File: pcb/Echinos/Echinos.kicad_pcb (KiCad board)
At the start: 4 copper layers, 139.8 x 117.6 mm, 132 parts, among them J1 USB_C_Receptacle_USB2.0, J206 Conn_01x06_Pin, J3 TagConnect_6pins, J301 SATA-7p, J4 FPC_VIK, SW1 SW_Push, SW101 RotaryEncoder_Switch, SW102 SW_Push, SW103 SW_Push, SW105 SW_Push, SW106 SW_Push, SW107 SW_Push, SW108 SW_Push, SW109 SW_Push, SW110 SW_Push, SW111 SW_Push, SW112 SW_Push, SW113 SW_Push, SW114 SW_Push, SW115 SW_Push, SW116 SW_Push, SW117 SW_Push, SW118 SW_Push, SW119 SW_Push, SW120 SW_Push, SW2 SW_Push, U1 RP2040, U2 XC6210B332MR-G, U205 PMW3360DM-T2QU, U206 VRH1902LTX, U3 ESD7L5.0DT5G-N, U4 W25Q128JVS, U7 D3V3F4U6S-7, X1 ASE-12MHz

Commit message: 🚧 [PCB] - Backup of a specific layout around MCU. Modules moved to a specific schematic page.
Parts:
- removed H7, H8, H9: GuardHole, MountingHole:MountingHole_2.2mm_M2_Pad_Via
- added D205: D, Echinos:D_SOD123, F.Cu at (234.8, 92.7)
- added J205: ~, Connector_FFC-FPC:Hirose_FH12-12S-0.5SH_1x12-1MP_P0.50mm_Horizontal, F.Cu at (192.6, 110.6)
- added J207: FPC (module), Connector_FFC-FPC:Hirose_FH12-6S-0.5SH_1x06-1MP_P0.50mm_Horizontal, F.Cu at (226.4, 85.8)
- added J208: FPC (PCB), Connector_FFC-FPC:Hirose_FH12-12S-0.5SH_1x12-1MP_P0.50mm_Horizontal, F.Cu at (111.1, 168.6)
- added J209: Joystick, Echinos:Joystick_Alps_SKRHACE010, F.Cu at (226.4, 96.3)
- moved C206 37.5 mm to (203.3, 94.9)
- moved R207 37.5 mm to (203.3, 102.4)
- moved U205 37.5 mm to (193.8, 97.2)
- moved C205 37.5 mm to (203.3, 92.4)
- moved C207 37.5 mm to (203.3, 97.4)
- moved C208 37.5 mm to (203.3, 99.9)
- moved R208 37.5 mm to (203.3, 104.9)
- moved U206 12.7 mm to (203.1, 109.7)
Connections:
- R208 pad 2: miso1 -> /Modules/miso
- U1 pad 8: /Left Side/RP2040_Left/GPIO6 -> row5
- U205 pad 10: sck1 -> /Modules/sck
- U205 pad 11: mosi1 -> /Modules/mosi
- U205 pad 12: miso1 -> /Modules/miso
- U205 pad 13: csn1 -> /Modules/csn
- U205 pad 9: motion -> /Modules/motion
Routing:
- net row5: track 0.00 -> 18.7 mm, vias 0 -> 1
- net /Left Side/RP2040_Left/GPIO6: track 18.7 -> 0.00 mm, vias 1 -> 0

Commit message: ✨ [PCB] - Make some place to add a FPC connector providing a way to expand the matrix / number of keys or add a joystick and I2C pull-up resistors. Improve routing in order to minimize the number of vias.
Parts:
- R14, R15: footprint Resistor_SMD:R_0805_2012Metric_Pad1.20x1.40mm_HandSolder -> Resistor_SMD:R_0402_1005Metric_Pad0.72x0.64mm_HandSolder
- moved JP2 220.6 mm to (128.6, 145.5), turned to 90 degrees
- moved R14 218.5 mm to (131.2, 144.3), turned to -90 degrees
- moved R15 213.4 mm to (128.6, 142.8), turned to -90 degrees
- moved J208 35.0 mm to (108.3, 133.8), turned to 0 degrees
- moved R13 23.1 mm to (67.2, -72.5), turned to -90 degrees
- moved C1 14.0 mm to (137.2, 136.1), turned to -90 degrees
- moved R2 12.1 mm to (137.2, 133.8)
- moved X1 9.64 mm to (134.0, 134.5), turned to 180 degrees
- moved JP1 7.39 mm to (90.4, -71.5), turned to 90 degrees
- moved R10 3.76 mm to (118.5, 146.9), turned to 90 degrees
- moved R11 3.68 mm to (115.7, 148.8)
- moved R8 3.44 mm to (125.2, 145.8), turned to -90 degrees
- moved C6 2.97 mm to (124.1, 144.5)
- moved C16 2.97 mm to (110.4, 149.1)
- moved U4 2.97 mm to (113.1, 145.2)
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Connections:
- J206 pad 3: sck0 -> mosi0
- J206 pad 4: mosi0 -> miso0
- J206 pad 5: miso0 -> csn0
- J206 pad 6: csn0 -> sck0
- U1 pad 2: rotB -> row5
- U1 pad 3: rotA -> rotB
- U1 pad 4: sck0 -> rotA
- U1 pad 8: row5 -> sck0
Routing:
- net col5: track 155.1 -> 179.4 mm, vias 1 -> 3
- net col4: track 178.1 -> 198.2 mm, vias 1 -> 3
- net col3: track 168.6 -> 188.7 mm
- net row5: track 18.7 -> 38.2 mm, vias 1 -> 2
- net +3.3V: track 309.2 -> 322.5 mm, vias 12 -> 10
- net col2: track 134.6 -> 147.8 mm, vias 1 -> 2
- net adc_1: track 116.8 -> 129.5 mm
- net adc_0: track 110.0 -> 120.1 mm
- net adc_3: track 30.7 -> 40.6 mm
- net /Left Side/SWIO: track 40.3 -> 33.2 mm
- net mosi0: track 16.3 -> 22.4 mm
- net miso0: track 14.6 -> 20.4 mm
- net csn0: track 12.8 -> 18.6 mm
- net Net-(U1-XIN): track 4.43 -> 9.96 mm
- net rotB: track 76.7 -> 82.1 mm
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
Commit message: 🚧 [PCB] - Backup before trying to add 5.0V support.
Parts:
- removed JW108: Joystick, Echinos:Joystick_KSilver_JP19
- added ?: , , F.Cu at (216.8, 98.6)
- added ?: , , F.Cu at (189.2, 98.6)
- added H6: MountHole, Echinos:MountingHole_3mm_Pad_Via, F.Cu at (212.7, 132.2)
- added J1002: Conn_01x06_Female, Connector_PinHeader_2.54mm:PinHeader_1x06_P2.54mm_Vertical, F.Cu at (192.8, 117.3)
- added J1002: Conn_01x06_Female, Connector_PinHeader_2.54mm:PinHeader_1x06_P2.54mm_Vertical, F.Cu at (213.2, 117.1)
- added JP206: i2c1_pullUp, Echinos:SolderJumper_Open_0.8x1.2mm, F.Cu at (2.26, -104.6)
- added R209: 4.7k, Resistor_SMD:R_0402_1005Metric_Pad0.72x0.64mm_HandSolder, F.Cu at (1.95, -93.5)
- added R210: 4.7k, Resistor_SMD:R_0402_1005Metric_Pad0.72x0.64mm_HandSolder, F.Cu at (1.95, -91.5)
- added REF**: vik-module-mounting-small, VIK:vik-module-mounting-small, F.Cu at (203.0, 98.6)
- J206: footprint Connector_PinHeader_2.54mm:PinHeader_1x06_P2.54mm_Vertical -> Connector_PinSocket_2.00mm:PinSocket_1x06_P2.00mm_Horizontal
- U206: value VRH1902LTX -> XC6206P202MR-G; footprint Package_TO_SOT_SMD:SOT-23-5_HandSoldering -> Package_TO_SOT_SMD:SOT-23-3
- moved D205 298.2 mm to (3.66, -95.8)
- moved J207 298.2 mm to (-4.72, -102.7)
- moved J209 298.2 mm to (-4.73, -92.2)
- moved J205 31.2 mm to (209.0, 84.1), turned to 90 degrees
- moved U206 26.4 mm to (195.8, 84.3)
- moved D120 22.9 mm to (190.9, 160.1)
- moved R208 19.8 mm to (201.8, 85.2), turned to -90 degrees
- moved R207 15.5 mm to (195.6, 89.0)
- moved C208 15.0 mm to (195.5, 87.1)
- moved C207 13.0 mm to (198.9, 85.2), turned to -90 degrees
- moved H1 11.9 mm to (212.8, 160.1)
- moved U205 9.24 mm to (203.0, 98.6)
- moved C206 9.00 mm to (194.7, 92.2), turned to 180 degrees
- moved C205 8.78 mm to (194.7, 94.1), turned to 180 degrees
- moved FB2 8.31 mm to (202.7, 153.3)
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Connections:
- net /Left Side/Matrix_Left/joy_108_out renamed Net-(D108-A)
- C207 pad 1: +3.3V -> /Modules/+3.3V_Ball
- C208 pad 1: VDD -> /Modules/VDD_Ball
- D1 pad 2: Net-(D1-A) -> VBUS_Fused
- F1 pad 2: Net-(D1-A) -> VBUS_Fused
- J205 pad 12: +3.3V -> /Modules/+3.3V_Ball
- J208 pad 8: rgb -> adc_0
- J208 pad 9: adc_0 -> rgb
- R205 pad 2: +5V -> VBUS_Fused
- R207 pad 1: VDD -> /Modules/VDD_Ball
- R208 pad 1: +3.3V -> /Modules/+3.3V_Ball
- U205 pad 4: VDD -> /Modules/VDD_Ball
- U205 pad 5: +3.3V -> /Modules/+3.3V_Ball
- U206 pad 1: +3.3V -> GND
- U206 pad 2: GND -> /Modules/VDD_Ball
- U206 pad 3: +3.3V -> /Modules/+3.3V_Ball
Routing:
- net VBUS_Fused: track 0.00 -> 106.2 mm, vias 0 -> 4
- net +5V: track 115.6 -> 11.9 mm, vias 4 -> 0
- net rgb: track 16.1 -> 45.3 mm, vias 2 -> 3
- net row4: track 111.5 -> 88.8 mm, vias 5 -> 4
- net /Left Side/Matrix_Left/joy_120_out: track 3.28 -> 25.0 mm, vias 0 -> 2
- net Net-(D108-A): track 38.3 -> 19.4 mm
- net +3.3V: track 322.5 -> 309.4 mm
- net adc_1: track 129.5 -> 116.5 mm, vias 3 -> 2
- net /Modules/+3.3V_Ball: track 0.00 -> 11.5 mm
- net Net-(U205-VDDPIX): track 0.00 -> 5.82 mm
- net /Modules/miso: track 0.00 -> 5.50 mm
- net adc_0: track 120.1 -> 115.1 mm
- net col2: track 147.8 -> 143.9 mm
- net /Modules/VDD_Ball: track 0.00 -> 3.71 mm
- net col3: track 188.7 -> 185.3 mm
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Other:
- board size 139.8 x 117.6 mm -> 143.4 x 117.6 mm
- board text added: "Kiwano V1.1"

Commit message: ✨ 🚧 [PCB] - Halves are now connected with 5.0V power to be able to expose it to modules (see VIK standard). Update the whole routing to make this happens. VBUS and 5.0V are now split with a schottky diode to still be able to detect when USB is plugged but avoid reverse current in case power comes from the other half. Add ESD events protection to SATA connector.
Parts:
- removed ? (x2): , 
- removed J1002 (x2): Conn_01x06_Female, Connector_PinHeader_2.54mm:PinHeader_1x06_P2.54mm_Vertical
- removed JP1: i2c0_pullUp, Echinos:SolderJumper_Open_0.8x1.2mm
- removed the R12 at (91.0, -80.3)
- removed the R13 at (67.2, -72.5)
- removed REF**: vik-module-mounting-small, VIK:vik-module-mounting-small
- added D4: 1N4148, Diode_SMD:D_SOD-323_HandSoldering, F.Cu at (146.3, 138.5)
- added F2: 500mA, Fuse:Fuse_0603_1608Metric_Pad1.05x0.95mm_HandSolder, F.Cu at (203.7, 150.7)
- U7: value D3V3F4U6S-7 -> SRV05-4; footprint Echinos:D_TVS_SOT-363 -> Package_TO_SOT_SMD:SOT-23-6
- moved D3 84.0 mm to (131.1, 150.2), turned to 0 degrees
- moved C14 82.6 mm to (126.0, 151.9), turned to 0 degrees
- moved R9 82.5 mm to (132.0, 148.7), turned to 180 degrees
- moved JP205 79.1 mm to (132.0, 146.7), turned to -90 degrees
- moved D1 77.6 mm to (122.4, 152.1), turned to 90 degrees
- moved U2 77.2 mm to (126.5, 149.1), turned to 0 degrees
- moved C15 74.5 mm to (129.9, 145.8), turned to 90 degrees
- moved C2 16.1 mm to (144.1, 139.8), turned to 180 degrees
- moved J3 15.1 mm to (143.4, 154.1), turned to 0 degrees
- moved R3 15.0 mm to (144.6, 137.7)
- moved R8 13.1 mm to (137.6, 150.3), turned to 0 degrees
- moved J206 7.16 mm to (109.1, 151.5), turned to 90 degrees
- moved C16 6.26 mm to (104.9, 146.1), turned to 90 degrees
- moved R4 6.09 mm to (116.5, 138.2)
- moved R5 6.03 mm to (116.5, 137.2)
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- renumbered J208 to J2, J301 to J5, R205 to R12, R206 to R13
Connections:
- net /Left Side/QSPI_SCLK renamed /Left Side/RP2040_Left/QSPI_SCLK
- net /Left Side/QSPI_SD0 renamed /Left Side/RP2040_Left/QSPI_SD0
- net /Left Side/QSPI_SD1 renamed /Left Side/RP2040_Left/QSPI_SD1
- net /Left Side/QSPI_SD2 renamed /Left Side/RP2040_Left/QSPI_SD2
- net /Left Side/QSPI_SD3 renamed /Left Side/RP2040_Left/QSPI_SD3
- net /Left Side/QSPI_SS renamed /Left Side/RP2040_Left/QSPI_SS
- net /Left Side/~{RST} renamed /Left Side/RP2040_Left/~{RST}
- D2 pad 1: +5V -> VBUS_Fused
- J2 pad 10: unconnected-(J208-Pin_10-Pad10) -> adc_1
- J2 pad 2: col2 -> col3
- J2 pad 3: col3 -> col4
- J2 pad 4: col4 -> col5
- J2 pad 5: row5 -> col2
- J2 pad 6: col5 -> row5
- J2 pad 7: adc_1 -> unconnected-(J2-Pin_7-Pad7)
- J2 pad 8: adc_0 -> rgb
- J2 pad 9: rgb -> adc_0
- J3 pad 2: /Left Side/SWIO -> /Left Side/RP2040_Left/SWDIO
- J3 pad 4: /Left Side/SWCLK -> /Left Side/RP2040_Left/SWCLK
- J4 pad 6: unconnected-(J4-Pin_6-Pad6) -> +5V
- J4 pad 7: adc_3 -> adc_2
- J4 pad 9: adc_2 -> adc_3
- J5 pad 2: +3.3V -> RX
- J5 pad 3: +3.3V -> TX
- J5 pad 5: RX -> VBUS_split
- J5 pad 6: TX -> VBUS_split
- JW120 pad 1: adc_0 -> adc_1
- JW120 pad 4: adc_1 -> adc_0
- U1 pad 24: /Left Side/SWIO -> /Left Side/RP2040_Left/SWCLK
- U1 pad 25: /Left Side/SWCLK -> /Left Side/RP2040_Left/SWDIO
- U7 pad 2: +3.3V -> GND
- U7 pad 5: GND -> VBUS_split
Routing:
- net +3.3V: track 309.4 -> 184.3 mm
- net +5V: track 11.9 -> 106.9 mm
- net /Left Side/RP2040_Left/SWDIO: track 0.00 -> 45.5 mm, vias 0 -> 2
- net /Left Side/RP2040_Left/SWCLK: track 0.00 -> 40.8 mm, vias 0 -> 2
- net /Left Side/SWCLK: track 35.1 -> 0.00 mm, vias 2 -> 0
- net /Left Side/SWIO: track 33.2 -> 0.00 mm, vias 2 -> 0
- net /Left Side/Matrix_Left/joy_120_out: track 25.0 -> 57.5 mm, vias 2 -> 4
- net /Left Side/RP2040_Left/~{RST}: track 55.9 -> 81.1 mm
- net col5: track 179.2 -> 196.5 mm
- net VBUS_split: track 0.00 -> 10.0 mm
- net col3: track 185.3 -> 195.3 mm, vias 1 -> 2
- net miso0: track 21.9 -> 12.4 mm
- net mosi0: track 23.3 -> 14.1 mm
- net csn0: track 20.5 -> 11.5 mm
- net GND: track 43.0 -> 34.2 mm, vias 61 -> 27
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- added copper zone on F.Cu, net +3.3V
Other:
- board size 143.4 x 117.6 mm -> 143.8 x 117.6 mm

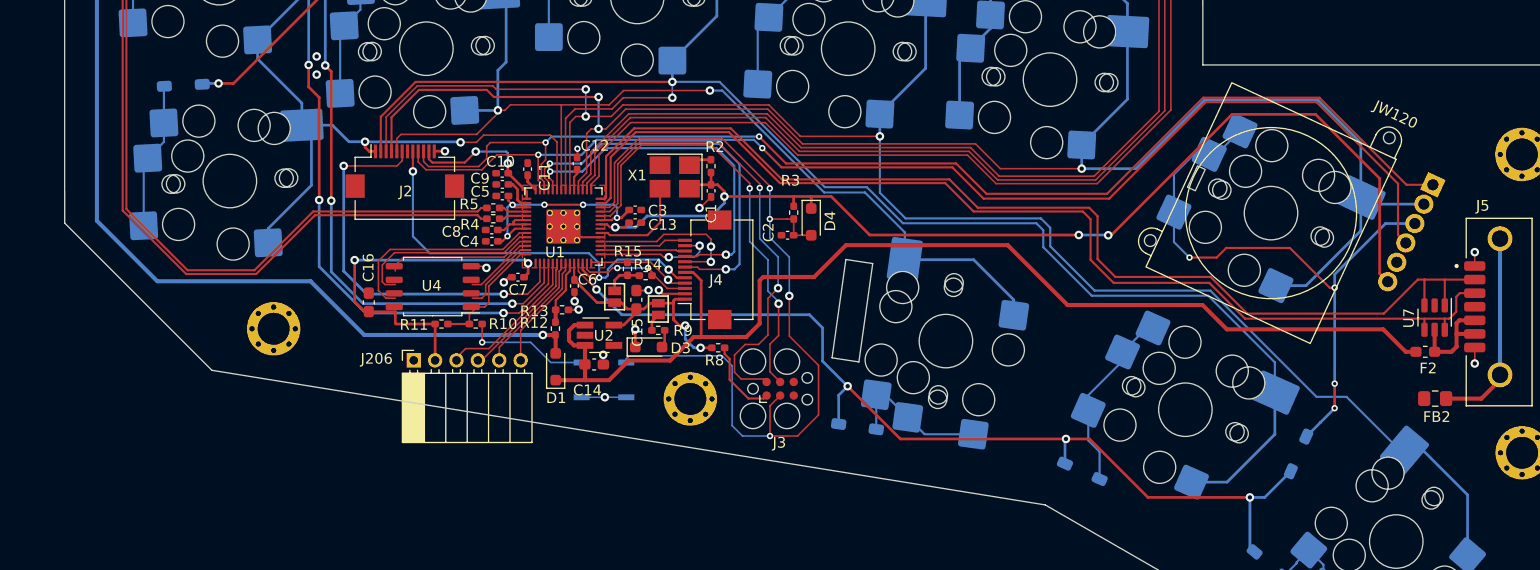
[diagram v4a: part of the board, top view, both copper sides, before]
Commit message: ♻️ [PCB] - Now using WSON package for flash memory chip to reduce component height. This allows FPC and memory to be closer freeing pcb space for 6 pins header.
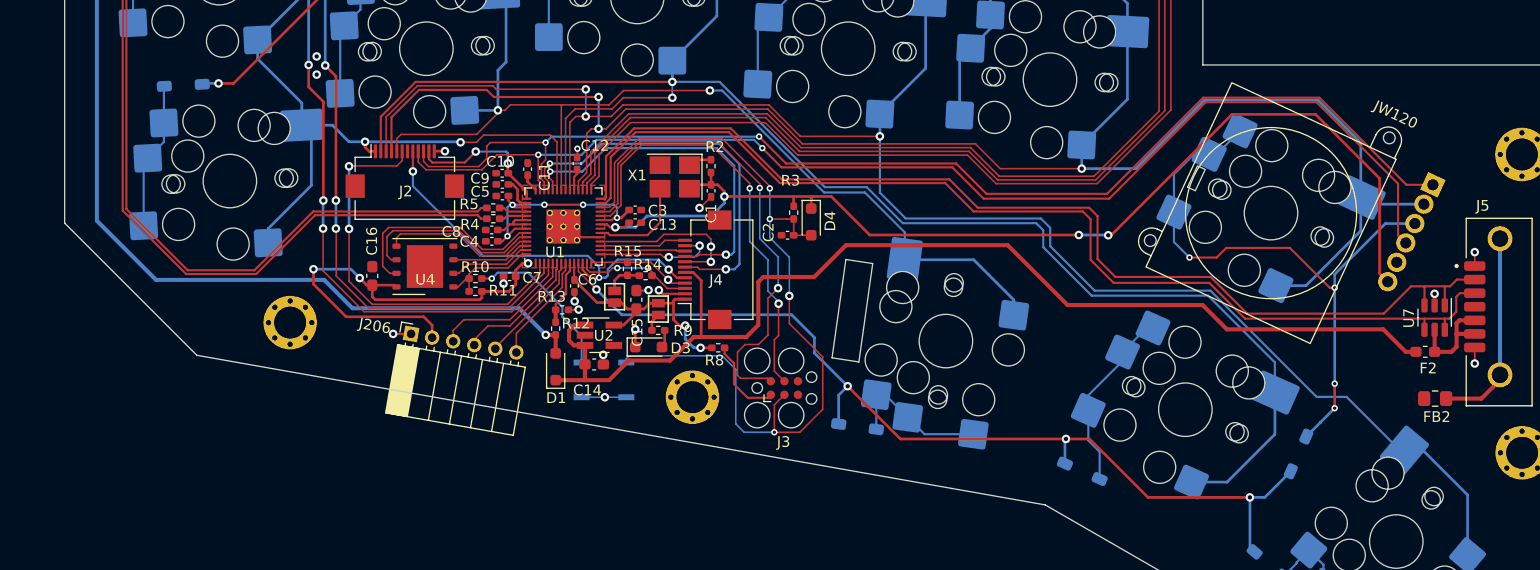
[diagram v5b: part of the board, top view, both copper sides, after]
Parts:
- U4: footprint Package_SO:SOIC-8_5.23x5.23mm_P1.27mm -> Package_SON:WSON-8-1EP_6x5mm_P1.27mm_EP3.4x4mm
- moved R11 4.40 mm to (114.9, 145.0), turned to 0 degrees
- moved R10 4.25 mm to (114.9, 143.8)
- moved C16 2.50 mm to (105.2, 143.6)
- moved J206 2.49 mm to (108.8, 149.0), turned to 80 degrees
- moved U4 2.01 mm to (110.2, 142.7)
- moved H3 1.65 mm to (97.5, 147.9)
- moved C7 0.78 mm to (118.1, 143.7)
- moved J3 0.40 mm to (143.8, 154.1)
- moved H5 0.26 mm to (135.2, 154.9)
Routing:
- net +3.3V: track 184.3 -> 192.2 mm, vias 10 -> 11
- net Net-(R10-Pad1): track 11.8 -> 15.0 mm
- net rgb: track 40.0 -> 37.0 mm
- net /Left Side/RP2040_Left/QSPI_SS: track 11.5 -> 9.55 mm
- net RX: track 102.4 -> 101.2 mm
- net row4: track 90.5 -> 89.5 mm
- net GND: track 34.2 -> 35.1 mm, vias 27 -> 28
- net csn0: track 11.5 -> 10.5 mm
- net /Left Side/RP2040_Left/QSPI_SD2: track 6.59 -> 7.39 mm
- net /Left Side/RP2040_Left/QSPI_SD0: track 13.7 -> 14.5 mm
- net /Left Side/RP2040_Left/~{RST}: track 81.1 -> 80.4 mm
- net sck0: track 10.8 -> 10.2 mm
- net rotA: track 71.3 -> 70.7 mm
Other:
- outline, holes or cut-outs redrawn
